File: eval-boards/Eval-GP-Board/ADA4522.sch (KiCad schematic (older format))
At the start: 13 parts, among them J4 TP1, J5 TP2, U1 ADA4522-1

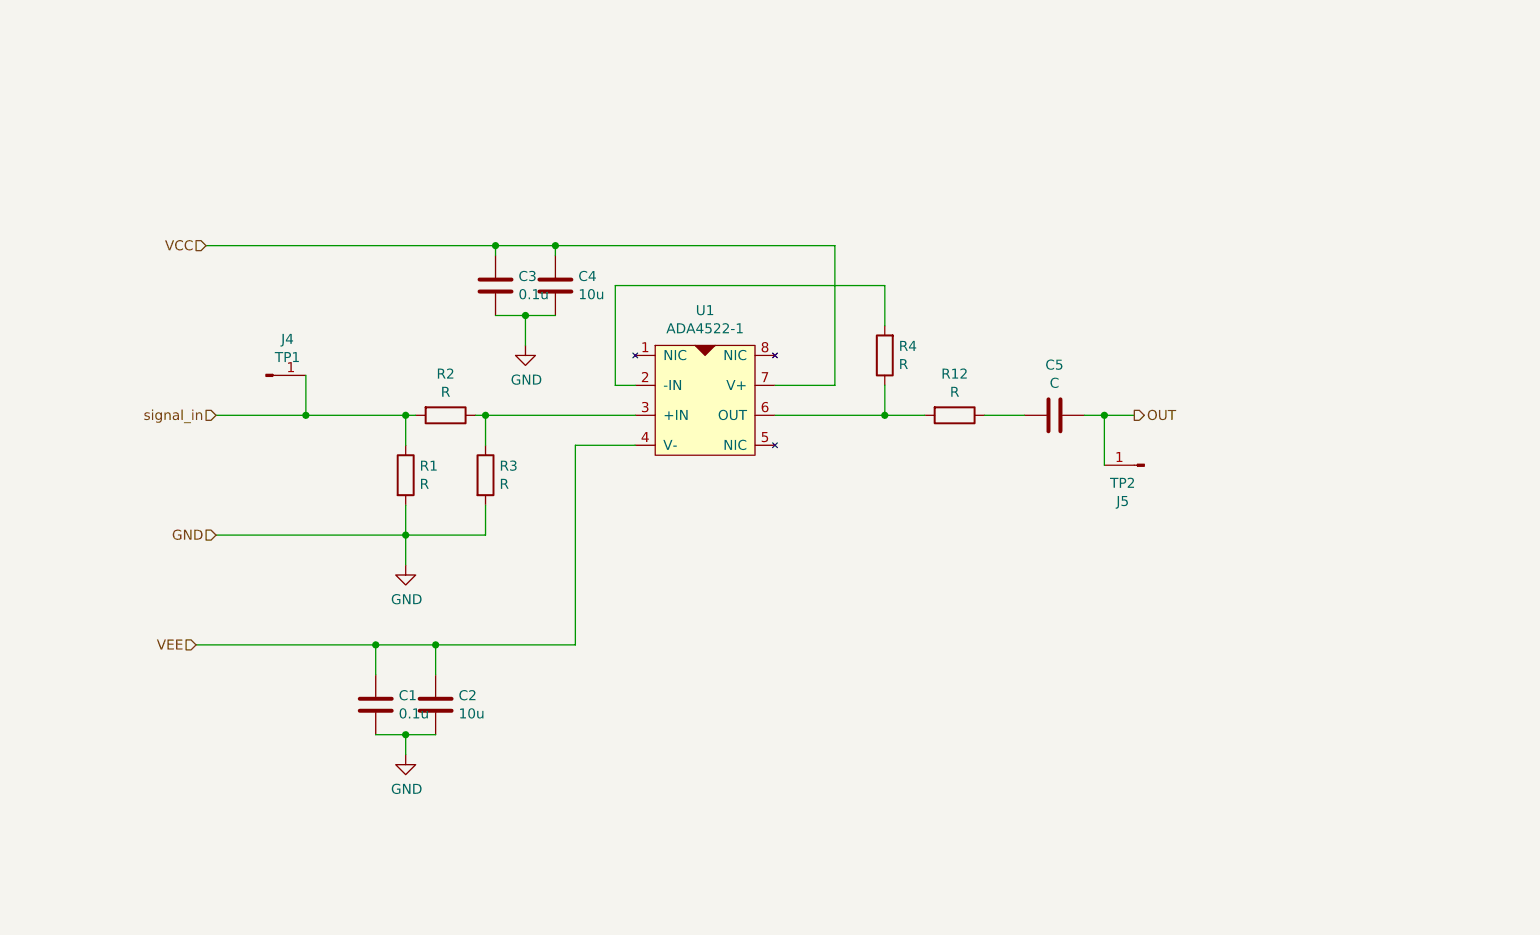
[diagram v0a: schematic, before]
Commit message: Updated schematic
均采用双运放，前级4522可以单运放工作也可以级联工作
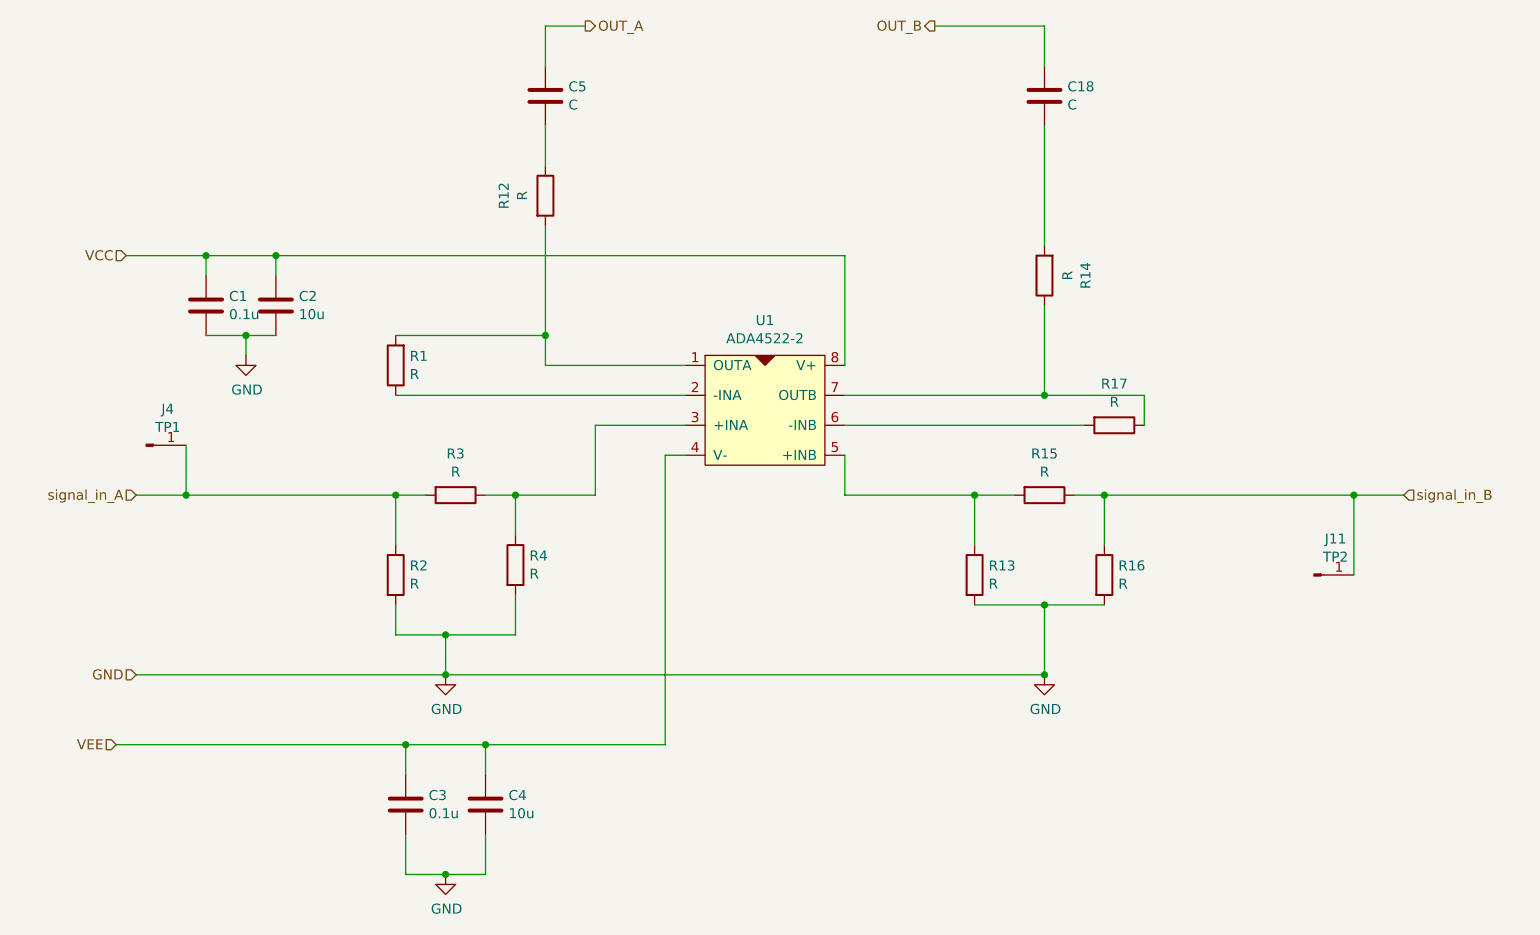
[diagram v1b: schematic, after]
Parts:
- removed J5: TP2, TestPoint:TestPoint_Pad_D2.0mm, symbol Connector:Conn_01x01_Male
- removed U1: ADA4522-1, Package_SO:SOIC-8_3.9x4.9mm_P1.27mm, symbol Amplifier_Operational:ADA4522-1
- added C18: C, Capacitor_SMD:C_0603_1608Metric, symbol Device:C
- added J11: TP2, TestPoint:TestPoint_Pad_D2.0mm, symbol Connector:Conn_01x01_Male
- added R13, R14, R15, R16, R17: R, Resistor_SMD:R_0603_1608Metric, symbol Device:R
- added U1: ADA4522-2, Package_SO:SOIC-8_3.9x4.9mm_P1.27mm, symbol Amplifier_Operational:ADA4522-2
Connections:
- net GND: now also R2.2, R4.2, R13.2, R16.2; no longer R1.2, R3.2
- net VCC: now also C1.1, C2.1, U1.8 (V+); no longer C3.1, C4.1
- net VEE: now also C3.1, C4.1, U1.4 (V-); no longer C1.1, C2.1
- net at R3.1: now also R4.1, U1.3 (+INA); no longer R2.1
- net at R12.2: now also R1.2, U1.1 (OUTA); no longer R4.1
- net OUT renamed OUT_A
- removed net signal_in: J4.1 (Pin_1), R1.1, R2.2
- new net: R1.1, U1.2 (-INA)
- new net: R13.1, R15.2, U1.5 (+INB)
- new net: R17.2, U1.6 (-INB)
- new net: R14.1, R17.1, U1.7 (OUTB)
- new net: C18.2, R14.2
- new net OUT_B: C18.1
- new net signal_in_A: J4.1 (Pin_1), R2.1, R3.2
- new net signal_in_B: J11.1 (Pin_1), R15.1, R16.1
